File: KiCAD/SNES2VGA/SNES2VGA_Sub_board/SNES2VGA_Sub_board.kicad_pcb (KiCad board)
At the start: 2 copper layers, 19.9 x 7.3 mm, 1 part, among them P1 AVMulti_SUB

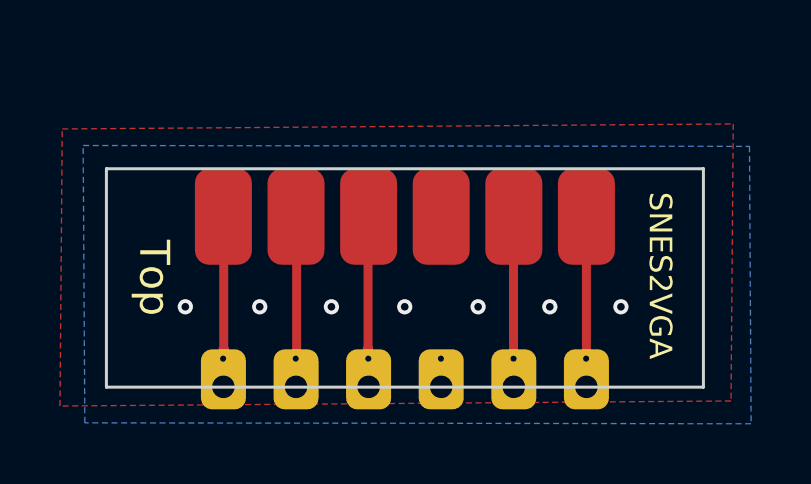
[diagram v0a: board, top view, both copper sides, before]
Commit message: Update to KiCad 9
 - Use kicad symbols and footprints if possible
 - Add JLCPCB QR/number placement square/text
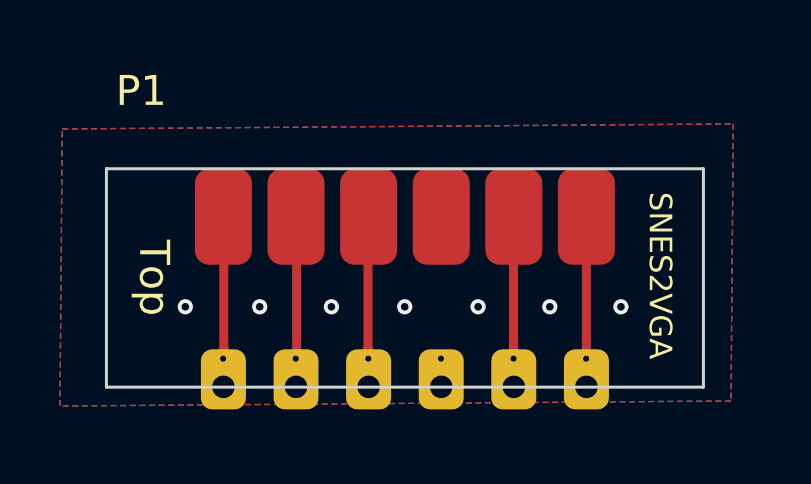
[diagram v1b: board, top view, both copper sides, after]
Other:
- net class Default removed
- net class Track removed
- rule pad_to_mask_clearance: 0.0508 -> 0
- board text added: "JLCJLCJLCJLC"
